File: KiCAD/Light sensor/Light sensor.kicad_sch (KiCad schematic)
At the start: 24 parts, among them J1 USB_B_Micro, U1 Opamp_Quad, U2 3.8V LDO, U3 1.024 Vref

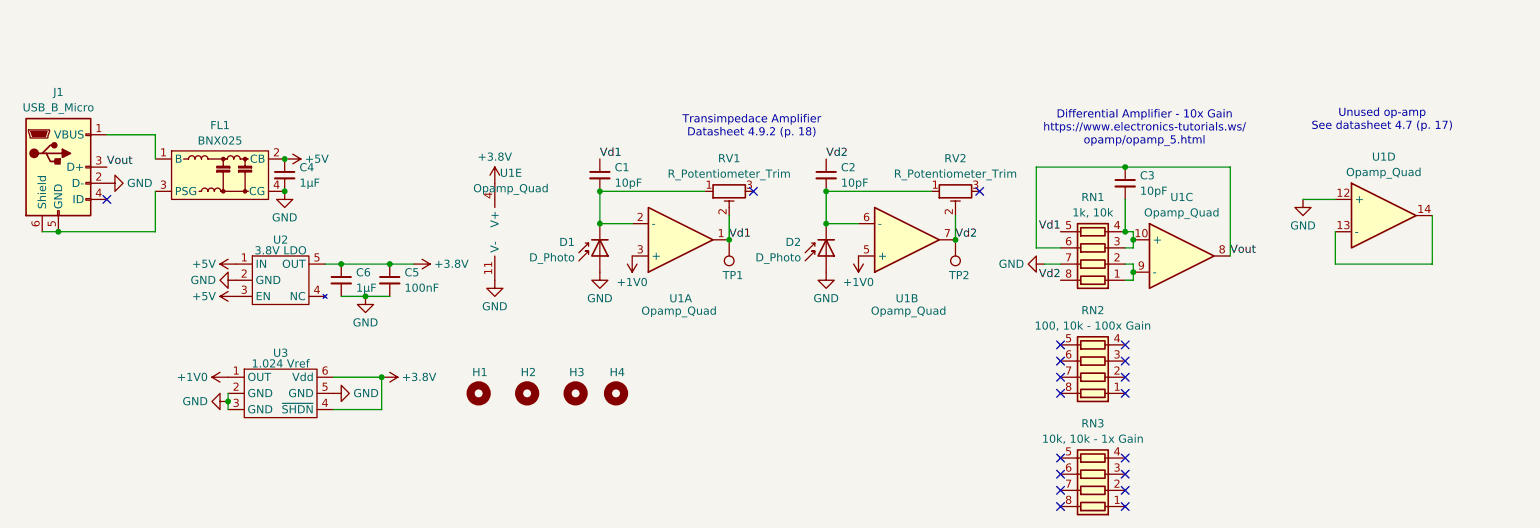
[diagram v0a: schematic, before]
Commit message: Add offset to diff amp, swap for better photodiodes
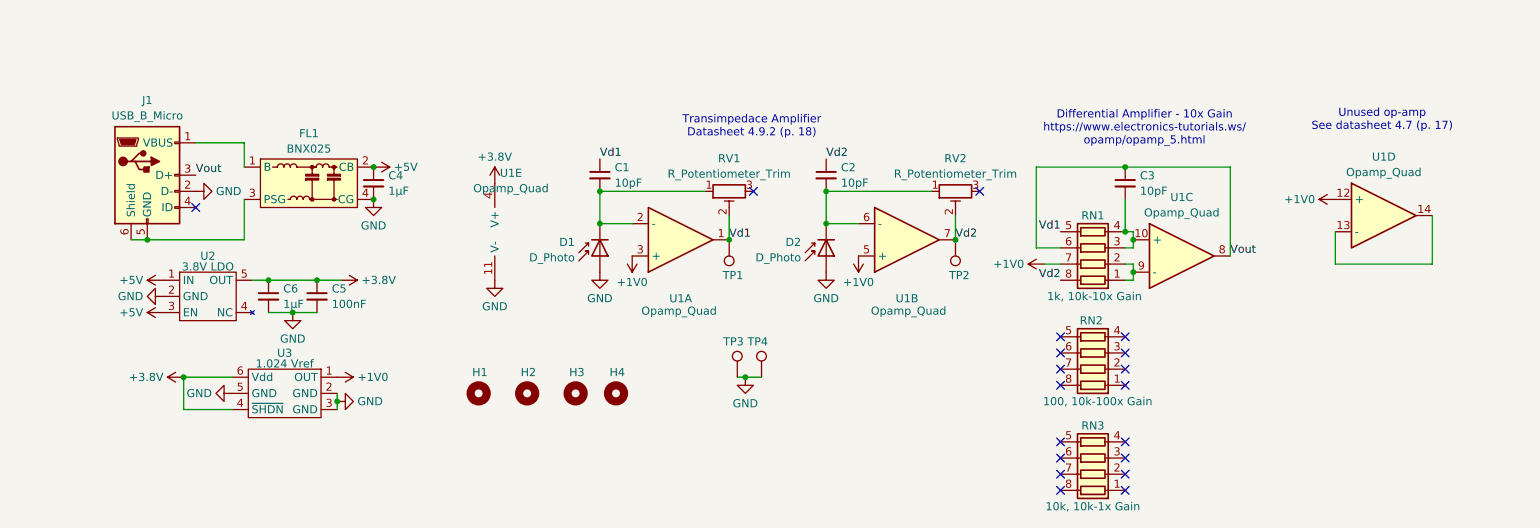
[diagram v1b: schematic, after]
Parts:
- added TP3, TP4: TestPoint, TestPoint:TestPoint_Pad_D3.0mm, symbol Connector:TestPoint
- D1, D2: footprint Custom:Photodiode -> Custom:XDCR_SFH_229; Part SFH 2716 A01 -> SFH 229
- RN1: value 1k, 10k -> 1k, 10k-10x Gain
- RN2: value 100, 10k - 100x Gain -> 100, 10k-100x Gain
- RN3: value 10k, 10k - 1x Gain -> 10k, 10k-1x Gain
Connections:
- net +1V0: now also RN1.7 (R2.2), U1.12 (+)
- net GND: now also TP3.1, TP4.1; no longer RN1.7 (R2.2), U1.12 (+)
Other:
- moved on the sheet: C4, C5, C6, FL1, J1, RN2, RN3, U2, U3

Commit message: Add coax connector for Vout
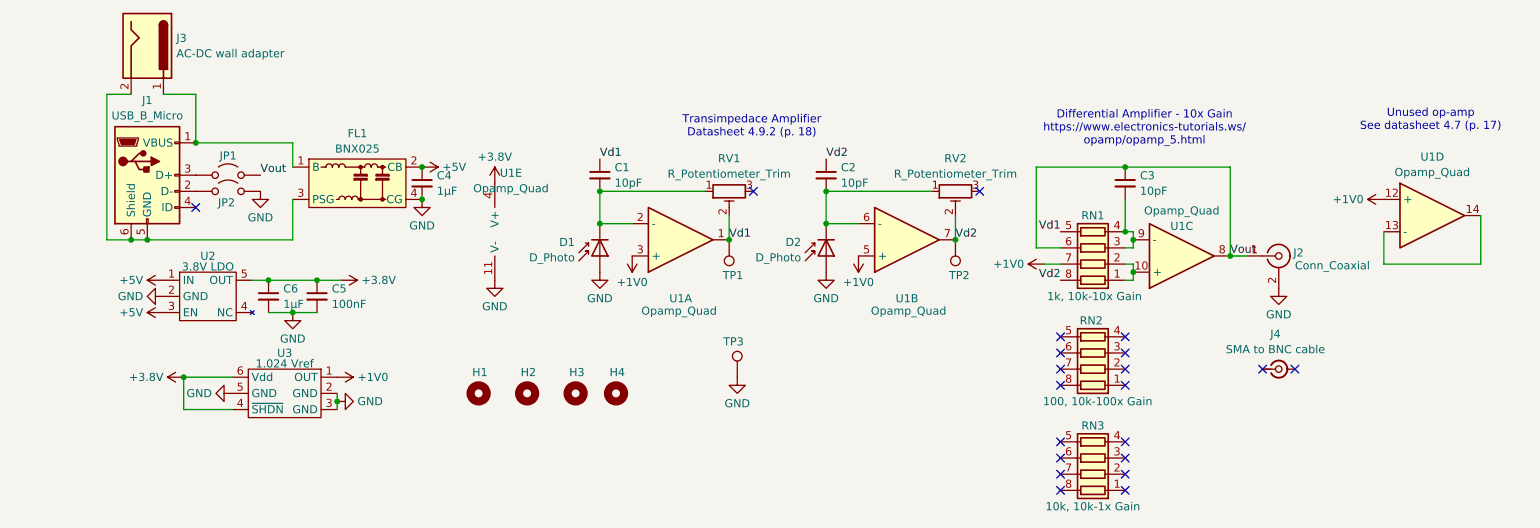
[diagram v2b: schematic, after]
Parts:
- removed TP4: TestPoint, TestPoint:TestPoint_Pad_D3.0mm, symbol Connector:TestPoint
- added J2: Conn_Coaxial, Custom:ADAMTECH_RF2-143-T-17-50-G, symbol Connector:Conn_Coaxial
- added J3: AC-DC wall adapter, symbol Connector:Jack-DC
- added J4: SMA to BNC cable, symbol Connector:Conn_Coaxial_Small
- added JP1, JP2: Jumper_2_Open, Jumper:SolderJumper-2_P1.3mm_Open_RoundedPad1.0x1.5mm, symbol Jumper:Jumper_2_Open
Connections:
- net GND: now also J2.2 (Ext), JP2.2 (B); no longer J1.2 (D-)
- net Vout: now also J2.1 (In), JP1.2 (B); no longer J1.3 (D+)
- net at FL1.1 (B), J1.1 (VBUS): now also J3.1
- net at FL1.3 (PSG), J1.5 (GND), J1.6 (Shield): now also J3.2
- net at RN1.1 (R1.1), RN1.2 (R2.1): now also U1.10 (+); no longer U1.9 (-)
- net at C3.2, RN1.3 (R3.1), RN1.4 (R4.1): now also U1.9 (-); no longer U1.10 (+)
- new net: J1.2 (D-), JP2.1 (A)
- new net: J1.3 (D+), JP1.1 (A)
- no-connect marks 19 -> 21
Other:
- moved on the sheet: C4, FL1, U1D
